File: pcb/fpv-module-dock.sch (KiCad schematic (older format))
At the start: 8 parts

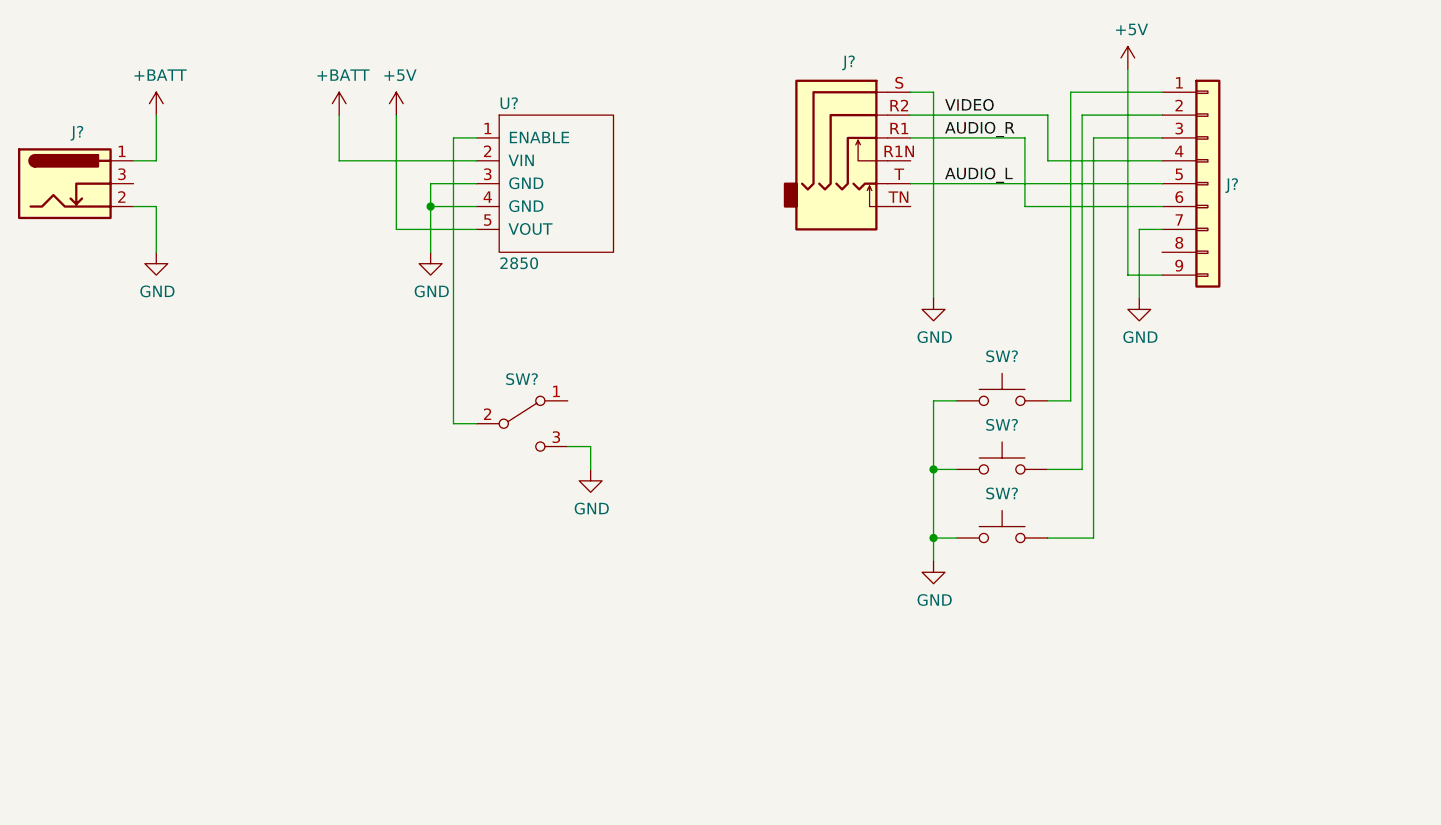
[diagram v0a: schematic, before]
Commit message: Schematic complete, exported netlist to layout
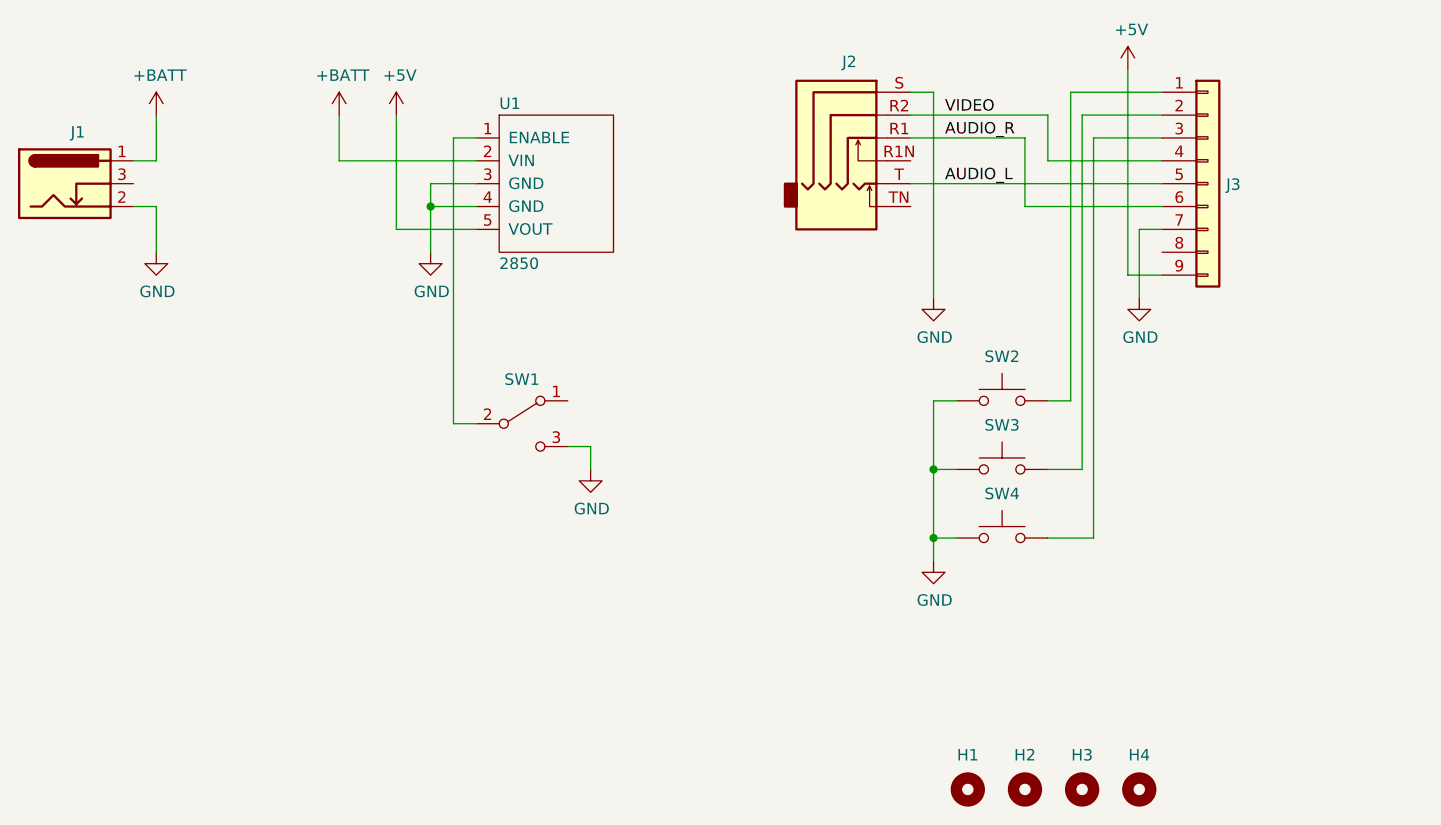
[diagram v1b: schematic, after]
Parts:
- added H1, H2, H3, H4: MountingHole, MountingHole:MountingHole_3.2mm_M3_Pad, symbol Mechanical:MountingHole
- SW1: renamed from SW?; footprint (none) -> Button_Switch_THT:SW_Slide_1P2T_CK_OS102011MS2Q
- SW2, SW3, SW4: renamed from SW?; footprint (none) -> Button_Switch_THT:SW_PUSH_6mm_H13mm
- U1: renamed from U?; footprint (none) -> fpv-module-dock:2850
- gave numbers to parts that had none: 3
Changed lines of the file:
@@
 $EndDescr
 $Comp
-L Connector:AudioJack4_SwitchTR1 J?
+L Connector:AudioJack4_SwitchTR1 J2
 U 1 1 60204525
 P 6300 3400
-F 0 "J?" H 6232 3733 50  0000 C CNN
+F 0 "J2" H 6232 3733 50  0000 C CNN
 F 1 "AudioJack4_SwitchTR1" H 6232 3734 50  0001 C CNN
 F 2 "fpv-module-dock:SJ-43516-SMT" H 6250 3400 50  0001 C CNN
@@
 $EndComp
 $Comp
-L Connector:Barrel_Jack_Switch J?
+L Connector:Barrel_Jack_Switch J1
 U 1 1 60205131
 P 2800 3600
-F 0 "J?" H 2857 3825 50  0000 C CNN
+F 0 "J1" H 2857 3825 50  0000 C CNN
 F 1 "Barrel_Jack_Switch" H 2857 3826 50  0001 C CNN
 F 2 "fpv-module-dock:PJ-051AH" H 2850 3560 50  0001 C CNN
@@
 $EndComp
 $Comp
-L Connector_Generic:Conn_01x09 J?
+L Connector_Generic:Conn_01x09 J3
 U 1 1 60206139
 P 7800 3600
-F 0 "J?" H 7880 3596 50  0000 L CNN
+F 0 "J3" H 7880 3596 50  0000 L CNN
 F 1 "Conn_01x09" H 7880 3551 50  0001 L CNN
 F 2 "Connector_PinSocket_2.54mm:PinSocket_1x09_P2.54mm_Vertical" H 7800 3600 50  0001 C CNN
@@
 $EndComp
 $Comp
-L power:GND #PWR?
+L power:GND #PWR010
 U 1 1 60206DD7
 P 7500 4100
-F 0 "#PWR?" H 7500 3850 50  0001 C CNN
+F 0 "#PWR010" H 7500 3850 50  0001 C CNN
 F 1 "GND" H 7505 3927 50  0000 C CNN
 F 2 "" H 7500 4100 50  0001 C CNN
@@
 $EndComp
 $Comp
-L power:+BATT #PWR?
+L power:+BATT #PWR01
 U 1 1 60207423
 P 3200 3300
-F 0 "#PWR?" H 3200 3150 50  0001 C CNN
+F 0 "#PWR01" H 3200 3150 50  0001 C CNN
 F 1 "+BATT" H 3215 3473 50  0000 C CNN
 F 2 "" H 3200 3300 50  0001 C CNN
@@
 $EndComp
 $Comp
-L power:GND #PWR?
+L power:GND #PWR02
 U 1 1 60207B56
 P 3200 3900
-F 0 "#PWR?" H 3200 3650 50  0001 C CNN
+F 0 "#PWR02" H 3200 3650 50  0001 C CNN
 F 1 "GND" H 3205 3727 50  0000 C CNN
 F 2 "" H 3200 3900 50  0001 C CNN
@@
 $EndComp
 $Comp
-L power:GND #PWR?
+L power:GND #PWR07
 U 1 1 60207E4C
 P 6600 4100
-F 0 "#PWR?" H 6600 3850 50  0001 C CNN
+F 0 "#PWR07" H 6600 3850 50  0001 C CNN
 F 1 "GND" H 6605 3927 50  0000 C CNN
 F 2 "" H 6600 4100 50  0001 C CNN
@@
 	7500 3800 7500 4100
 $Comp
-L power:+5V #PWR?
+L power:+5V #PWR09
 U 1 1 6020D921
 P 7450 3100
-F 0 "#PWR?" H 7450 2950 50  0001 C CNN
+F 0 "#PWR09" H 7450 2950 50  0001 C CNN
 F 1 "+5V" H 7465 3273 50  0000 C CNN
 F 2 "" H 7450 3100 50  0001 C CNN
@@
 	7450 4000 7600 4000
 $Comp
-L Switch:SW_Push SW?
+L Switch:SW_Push SW2
 U 1 1 6020FD90
 P 6900 4550
-F 0 "SW?" H 6900 4743 50  0000 C CNN
+F 0 "SW2" H 6900 4743 50  0000 C CNN
 F 1 "SW_Push" H 6900 4744 50  0001 C CNN
-F 2 "" H 6900 4750 50  0001 C CNN
+F 2 "Button_Switch_THT:SW_PUSH_6mm_H13mm" H 6900 4750 50  0001 C CNN
 F 3 "~" H 6900 4750 50  0001 C CNN
 F 4 "450-1642-ND‎" H 6900 4550 50  0001 C CNN "Digi-Key Part Number"
@@
 $EndComp
 $Comp
-L Switch:SW_Push SW?
+L Switch:SW_Push SW3
 U 1 1 602126F7
 P 6900 4850
-F 0 "SW?" H 6900 5043 50  0000 C CNN
+F 0 "SW3" H 6900 5043 50  0000 C CNN
 F 1 "SW_Push" H 6900 5044 50  0001 C CNN
-F 2 "" H 6900 5050 50  0001 C CNN
+F 2 "Button_Switch_THT:SW_PUSH_6mm_H13mm" H 6900 5050 50  0001 C CNN
 F 3 "~" H 6900 5050 50  0001 C CNN
 F 4 "450-1642-ND‎" H 6900 4850 50  0001 C CNN "Digi-Key Part Number"
@@
 $EndComp
 $Comp
-L Switch:SW_Push SW?
+L Switch:SW_Push SW4
 U 1 1 60212A6D
 P 6900 5150
-F 0 "SW?" H 6900 5343 50  0000 C CNN
+F 0 "SW4" H 6900 5343 50  0000 C CNN
 F 1 "SW_Push" H 6900 5344 50  0001 C CNN
-F 2 "" H 6900 5350 50  0001 C CNN
+F 2 "Button_Switch_THT:SW_PUSH_6mm_H13mm" H 6900 5350 50  0001 C CNN
 F 3 "~" H 6900 5350 50  0001 C CNN
 F 4 "450-1642-ND‎" H 6900 5150 50  0001 C CNN "Digi-Key Part Number"
@@
 $EndComp
 $Comp
-L power:GND #PWR?
+L power:GND #PWR08
 U 1 1 60214FE6
 P 6600 5250
-F 0 "#PWR?" H 6600 5000 50  0001 C CNN
+F 0 "#PWR08" H 6600 5000 50  0001 C CNN
 F 1 "GND" H 6605 5077 50  0000 C CNN
 F 2 "" H 6600 5250 50  0001 C CNN
@@
 VIDEO
 $Comp
-L Switch:SW_SPDT SW?
+L Switch:SW_SPDT SW1
 U 1 1 60229E96
 P 4800 4650
-F 0 "SW?" H 4800 4843 50  0000 C CNN
+F 0 "SW1" H 4800 4843 50  0000 C CNN
 F 1 "SW_SPDT" H 4800 4844 50  0001 C CNN
-F 2 "" H 4800 4650 50  0001 C CNN
+F 2 "Button_Switch_THT:SW_Slide_1P2T_CK_OS102011MS2Q" H 4800 4650 50  0001 C CNN
 F 3 "~" H 4800 4650 50  0001 C CNN
 F 4 "CKN9559-ND‎" H 4800 4650 50  0001 C CNN "Digi-Key Part Number"
@@
 $EndComp
 $Comp
-L power:GND #PWR?
+L power:GND #PWR06
 U 1 1 6022AD19
 P 5100 4850
-F 0 "#PWR?" H 5100 4600 50  0001 C CNN
+F 0 "#PWR06" H 5100 4600 50  0001 C CNN
 F 1 "GND" H 5105 4677 50  0000 C CNN
 F 2 "" H 5100 4850 50  0001 C CNN
@@
 	5100 4750 5100 4850
 $Comp
-L fpv-module-dock:2850 U?
+L fpv-module-dock:2850 U1
 U 1 1 6022C2F7
 P 4700 3600
-F 0 "U?" H 4700 3950 50  0000 L CNN
+F 0 "U1" H 4700 3950 50  0000 L CNN
 F 1 "2850" H 4700 3250 50  0000 L CNN
-F 2 "" H 4700 3600 50  0001 C CNN
+F 2 "fpv-module-dock:2850" H 4700 3600 50  0001 C CNN
 F 3 "" H 4700 3600 50  0001 C CNN
 F 4 "2183-2850-ND" H 4700 3600 50  0001 C CNN "Digi-Key Part Number"
@@
 $EndComp
 $Comp
-L power:+5V #PWR?
+L power:+5V #PWR04
 U 1 1 6022D1BB
 P 4250 3300
-F 0 "#PWR?" H 4250 3150 50  0001 C CNN
+F 0 "#PWR04" H 4250 3150 50  0001 C CNN
 F 1 "+5V" H 4265 3473 50  0000 C CNN
 F 2 "" H 4250 3300 50  0001 C CNN
@@
 $EndComp
 $Comp
-L power:+BATT #PWR?
+L power:+BATT #PWR03
 U 1 1 6022D64C
 P 4000 3300
-F 0 "#PWR?" H 4000 3150 50  0001 C CNN
+F 0 "#PWR03" H 4000 3150 50  0001 C CNN
 F 1 "+BATT" H 4015 3473 50  0000 C CNN
 F 2 "" H 4000 3300 50  0001 C CNN
@@
 	4000 3500 4000 3300
 $Comp
-L power:GND #PWR?
+L power:GND #PWR05
 U 1 1 6022ED1F
 P 4400 3900
-F 0 "#PWR?" H 4400 3650 50  0001 C CNN
+F 0 "#PWR05" H 4400 3650 50  0001 C CNN
 F 1 "GND" H 4405 3727 50  0000 C CNN
 F 2 "" H 4400 3900 50  0001 C CNN
@@
 Wire Wire Line
 	4500 4650 4500 3400
+$Comp
+L Mechanical:MountingHole H1
+U 1 1 60207227
+P 6750 6250
+F 0 "H1" H 6750 6400 50  0000 C CNN
+F 1 "MountingHole" H 6850 6205 50  0001 L CNN
+F 2 "MountingHole:MountingHole_3.2mm_M3_Pad" H 6750 6250 50  0001 C CNN
+F 3 "~" H 6750 6250 50  0001 C CNN
+	1    6750 6250
+	1    0    0    -1
+$EndComp
+$Comp
+L Mechanical:MountingHole H2
+U 1 1 60209029
+P 7000 6250
+F 0 "H2" H 7000 6400 50  0000 C CNN
+F 1 "MountingHole" H 7100 6205 50  0001 L CNN
+F 2 "MountingHole:MountingHole_3.2mm_M3_Pad" H 7000 6250 50  0001 C CNN
+F 3 "~" H 7000 6250 50  0001 C CNN
+	1    7000 6250
+	1    0    0    -1
+$EndComp
+$Comp
+L Mechanical:MountingHole H3
+U 1 1 602091AF
+P 7250 6250
+F 0 "H3" H 7250 6400 50  0000 C CNN
+F 1 "MountingHole" H 7350 6205 50  0001 L CNN
+F 2 "MountingHole:MountingHole_3.2mm_M3_Pad" H 7250 6250 50  0001 C CNN
+F 3 "~" H 7250 6250 50  0001 C CNN
+	1    7250 6250
+	1    0    0    -1
+$EndComp
+$Comp
+L Mechanical:MountingHole H4
+U 1 1 60209384
+P 7500 6250
+F 0 "H4" H 7500 6400 50  0000 C CNN
+F 1 "MountingHole" H 7600 6205 50  0001 L CNN
+F 2 "MountingHole:MountingHole_3.2mm_M3_Pad" H 7500 6250 50  0001 C CNN
+F 3 "~" H 7500 6250 50  0001 C CNN
+	1    7500 6250
+	1    0    0    -1
+$EndComp
 $EndSCHEMATC

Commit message: Added 3D models, completed layout
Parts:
- H1, H2, H3, H4: footprint MountingHole:MountingHole_3.2mm_M3_Pad -> MountingHole:MountingHole_3.2mm_M3
- SW1: footprint Button_Switch_THT:SW_Slide_1P2T_CK_OS102011MS2Q -> fpv-module-dock:OS102011MA1QN1
- SW2, SW3, SW4: footprint Button_Switch_THT:SW_PUSH_6mm_H13mm -> Button_Switch_THT:SW_Tactile_SPST_Angled_PTS645Vx83-2LFS
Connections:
- net GND: now also SW1.1 (A); no longer SW1.3 (C)
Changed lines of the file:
@@
 F 0 "SW2" H 6900 4743 50  0000 C CNN
 F 1 "SW_Push" H 6900 4744 50  0001 C CNN
-F 2 "Button_Switch_THT:SW_PUSH_6mm_H13mm" H 6900 4750 50  0001 C CNN
+F 2 "Button_Switch_THT:SW_Tactile_SPST_Angled_PTS645Vx83-2LFS" H 6900 4750 50  0001 C CNN
 F 3 "~" H 6900 4750 50  0001 C CNN
 F 4 "450-1642-ND‎" H 6900 4550 50  0001 C CNN "Digi-Key Part Number"
@@
 F 0 "SW3" H 6900 5043 50  0000 C CNN
 F 1 "SW_Push" H 6900 5044 50  0001 C CNN
-F 2 "Button_Switch_THT:SW_PUSH_6mm_H13mm" H 6900 5050 50  0001 C CNN
+F 2 "Button_Switch_THT:SW_Tactile_SPST_Angled_PTS645Vx83-2LFS" H 6900 5050 50  0001 C CNN
 F 3 "~" H 6900 5050 50  0001 C CNN
 F 4 "450-1642-ND‎" H 6900 4850 50  0001 C CNN "Digi-Key Part Number"
@@
 F 0 "SW4" H 6900 5343 50  0000 C CNN
 F 1 "SW_Push" H 6900 5344 50  0001 C CNN
-F 2 "Button_Switch_THT:SW_PUSH_6mm_H13mm" H 6900 5350 50  0001 C CNN
+F 2 "Button_Switch_THT:SW_Tactile_SPST_Angled_PTS645Vx83-2LFS" H 6900 5350 50  0001 C CNN
 F 3 "~" H 6900 5350 50  0001 C CNN
 F 4 "450-1642-ND‎" H 6900 5150 50  0001 C CNN "Digi-Key Part Number"
@@
 F 0 "SW1" H 4800 4843 50  0000 C CNN
 F 1 "SW_SPDT" H 4800 4844 50  0001 C CNN
-F 2 "Button_Switch_THT:SW_Slide_1P2T_CK_OS102011MS2Q" H 4800 4650 50  0001 C CNN
+F 2 "fpv-module-dock:OS102011MA1QN1" H 4800 4650 50  0001 C CNN
 F 3 "~" H 4800 4650 50  0001 C CNN
 F 4 "CKN9559-ND‎" H 4800 4650 50  0001 C CNN "Digi-Key Part Number"
@@
 	1    0    0    -1
 $EndComp
-Wire Wire Line
-	5000 4750 5100 4750
-Wire Wire Line
-	5100 4750 5100 4850
 $Comp
 L fpv-module-dock:2850 U1
@@
 F 0 "H1" H 6750 6400 50  0000 C CNN
 F 1 "MountingHole" H 6850 6205 50  0001 L CNN
-F 2 "MountingHole:MountingHole_3.2mm_M3_Pad" H 6750 6250 50  0001 C CNN
+F 2 "MountingHole:MountingHole_3.2mm_M3" H 6750 6250 50  0001 C CNN
 F 3 "~" H 6750 6250 50  0001 C CNN
 	1    6750 6250
@@
 F 0 "H2" H 7000 6400 50  0000 C CNN
 F 1 "MountingHole" H 7100 6205 50  0001 L CNN
-F 2 "MountingHole:MountingHole_3.2mm_M3_Pad" H 7000 6250 50  0001 C CNN
+F 2 "MountingHole:MountingHole_3.2mm_M3" H 7000 6250 50  0001 C CNN
 F 3 "~" H 7000 6250 50  0001 C CNN
 	1    7000 6250
@@
 F 0 "H3" H 7250 6400 50  0000 C CNN
 F 1 "MountingHole" H 7350 6205 50  0001 L CNN
-F 2 "MountingHole:MountingHole_3.2mm_M3_Pad" H 7250 6250 50  0001 C CNN
+F 2 "MountingHole:MountingHole_3.2mm_M3" H 7250 6250 50  0001 C CNN
 F 3 "~" H 7250 6250 50  0001 C CNN
 	1    7250 6250
@@
 F 0 "H4" H 7500 6400 50  0000 C CNN
 F 1 "MountingHole" H 7600 6205 50  0001 L CNN
-F 2 "MountingHole:MountingHole_3.2mm_M3_Pad" H 7500 6250 50  0001 C CNN
+F 2 "MountingHole:MountingHole_3.2mm_M3" H 7500 6250 50  0001 C CNN
 F 3 "~" H 7500 6250 50  0001 C CNN
 	1    7500 6250
 	1    0    0    -1
 $EndComp
+Wire Wire Line
+	5000 4550 5100 4550
+Wire Wire Line
+	5100 4550 5100 4850
 $EndSCHEMATC

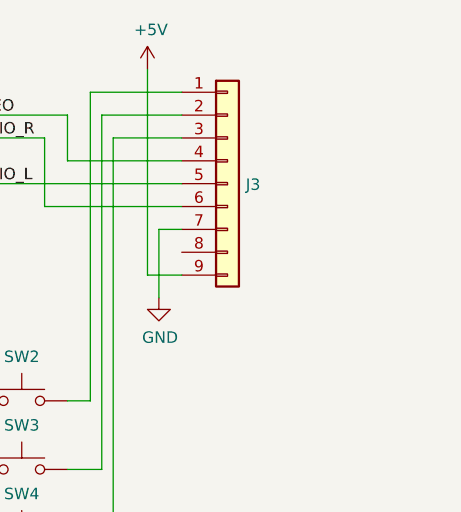
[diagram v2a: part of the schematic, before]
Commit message: Added power LED
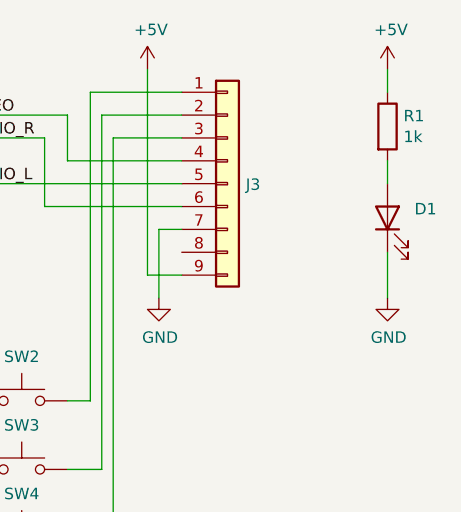
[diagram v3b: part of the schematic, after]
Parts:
- added D1: LED, LED_SMD:LED_0805_2012Metric_Pad1.15x1.40mm_HandSolder, symbol Device:LED
- added R1: 1k, Resistor_SMD:R_0805_2012Metric_Pad1.15x1.40mm_HandSolder, symbol Device:R
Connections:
- net +5V: now also R1.1
- net GND: now also D1.1 (K)
- new net: D1.2 (A), R1.2
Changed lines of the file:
@@
 Wire Wire Line
 	5100 4550 5100 4850
+$Comp
+L Device:LED D1
+U 1 1 60222634
+P 8500 3750
+F 0 "D1" V 8539 3632 50  0000 R CNN
+F 1 "LED" V 8448 3632 50  0001 R CNN
+F 2 "LED_SMD:LED_0805_2012Metric_Pad1.15x1.40mm_HandSolder" H 8500 3750 50  0001 C CNN
+F 3 "~" H 8500 3750 50  0001 C CNN
+F 4 "754-1132-1-ND" H 8500 3750 50  0001 C CNN "Digi-Key Part Number"
+	1    8500 3750
+	0    -1   -1   0
+$EndComp
+$Comp
+L power:+5V #PWR011
+U 1 1 602241AE
+P 8500 3100
+F 0 "#PWR011" H 8500 2950 50  0001 C CNN
+F 1 "+5V" H 8515 3273 50  0000 C CNN
+F 2 "" H 8500 3100 50  0001 C CNN
+F 3 "" H 8500 3100 50  0001 C CNN
+	1    8500 3100
+	1    0    0    -1
+$EndComp
+$Comp
+L Device:R R1
+U 1 1 602248EB
+P 8500 3350
+F 0 "R1" H 8570 3396 50  0000 L CNN
+F 1 "1k" H 8570 3305 50  0000 L CNN
+F 2 "Resistor_SMD:R_0805_2012Metric_Pad1.15x1.40mm_HandSolder" V 8430 3350 50  0001 C CNN
+F 3 "~" H 8500 3350 50  0001 C CNN
+F 4 "311-1.00KCRCT-ND" H 8500 3350 50  0001 C CNN "Digi-Key Part Number"
+	1    8500 3350
+	1    0    0    -1
+$EndComp
+$Comp
+L power:GND #PWR012
+U 1 1 60224D57
+P 8500 4100
+F 0 "#PWR012" H 8500 3850 50  0001 C CNN
+F 1 "GND" H 8505 3927 50  0000 C CNN
+F 2 "" H 8500 4100 50  0001 C CNN
+F 3 "" H 8500 4100 50  0001 C CNN
+	1    8500 4100
+	1    0    0    -1
+$EndComp
+Wire Wire Line
+	8500 3100 8500 3200
+Wire Wire Line
+	8500 3500 8500 3600
+Wire Wire Line
+	8500 3900 8500 4100
 $EndSCHEMATC
